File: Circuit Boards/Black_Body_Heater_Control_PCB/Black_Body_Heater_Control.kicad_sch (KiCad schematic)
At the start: 0 parts

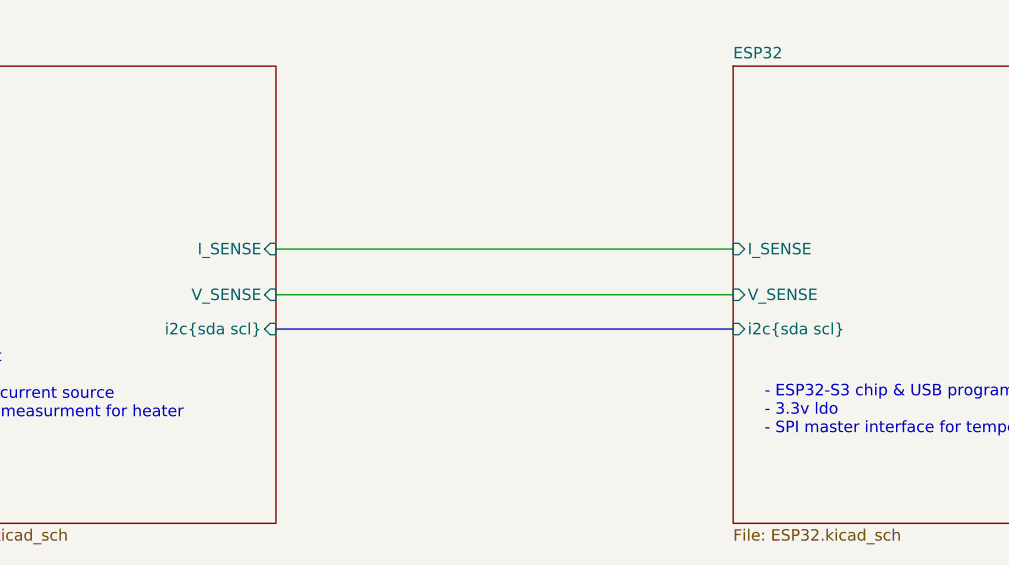
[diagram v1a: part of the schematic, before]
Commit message: Changing buck on heater pcb
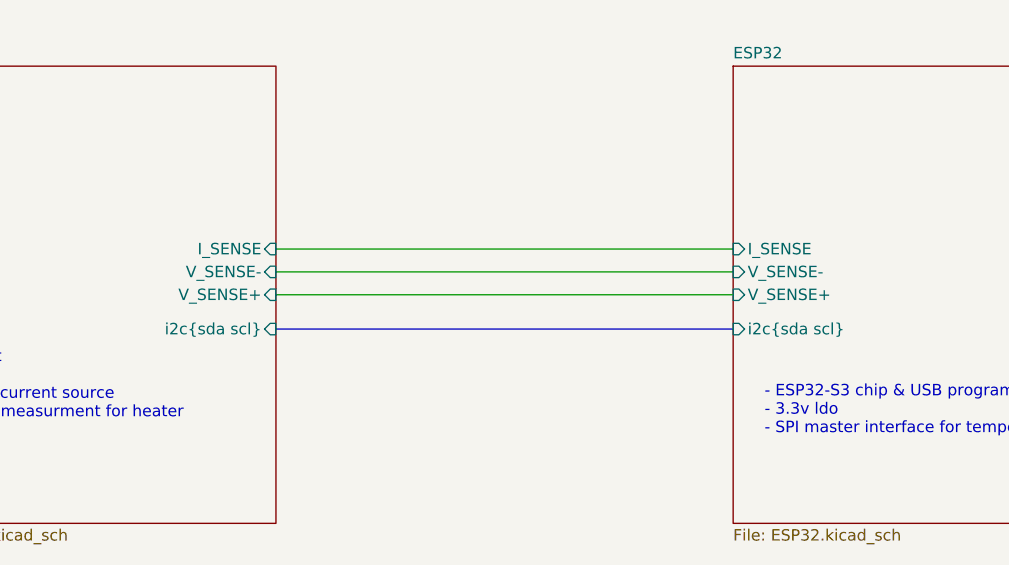
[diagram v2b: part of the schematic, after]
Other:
- sheet ESP32 ports: added V_SENSE+, V_SENSE-; removed V_SENSE
- sheet Power_periferals ports: added V_SENSE+, V_SENSE-; removed V_SENSE
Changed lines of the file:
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@@
+		)
+	)
+	(wire
+		(pts
+			(xy 129.54 97.79) (xy 180.34 97.79)
+		)
+		(stroke
+			(width 0)
+			(type default)
 		)
 	)
@@
 			)
 		)
-		(pin "V_SENSE" input
-			(at 129.54 100.33 0)
-			(effects
-				(font
-					(size 1.27 1.27)
-				)
-				(justify right)
-			)
-		)
 		(pin "I_SENSE" input
 			(at 129.54 95.25 0)
@@
 		(pin "i2c{sda scl}" input
 			(at 129.54 104.14 0)
+			(effects
+				(font
+					(size 1.27 1.27)
+				)
+				(justify right)
+			)
+		)
+		(pin "V_SENSE+" input
+			(at 129.54 100.33 0)
+			(effects
+				(font
+					(size 1.27 1.27)
+				)
+				(justify right)
+			)
+		)
+		(pin "V_SENSE-" input
+			(at 129.54 97.79 0)
 			(effects
 				(font
@@
 			)
 		)
-		(pin "V_SENSE" input
-			(at 180.34 100.33 180)
+		(pin "i2c{sda scl}" input
+			(at 180.34 104.14 180)
 			(effects
 				(font
@@
 			)
 		)
-		(pin "i2c{sda scl}" input
-			(at 180.34 104.14 180)
+		(pin "V_SENSE-" input
+			(at 180.34 97.79 180)
 			(effects
 				(font
+					(size 1.27 1.27)
+				)
+				(justify left)
+			)
+		)
+		(pin "V_SENSE+" input
+			(at 180.34 100.33 180)
+			(effects
+				(font
